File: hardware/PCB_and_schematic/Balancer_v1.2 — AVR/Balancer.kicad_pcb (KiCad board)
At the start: 2 copper layers, 99.5 x 99.5 mm, 198 parts, among them J1 BATT_OUT, J10 RS485, J11 HEATSING_TEMP1, J12 External Current Shunt, J13 BATT_IN, J14 LOAD_RESISTOR, J15 LOAD_RESISTOR, J16 ICP, J3 Conn_01x03, J4 HEATSING_TEMP1, J5 FAN1, J6 FAN2, J7 BATT_12V, J8 Conn_01x06, J9 RS485, Q1 BC817, Q10 BC807, Q11 BC817, Q12 BC817, Q13 BD238, Q14 BC807, Q15 BC817, Q16 BD238, Q18 IRF540N, Q2 BC817, Q23 BC817, Q25 IRF540N, Q3 BC807, Q4 PMOS, Q5 PMOS, Q6 BC817, Q7 BC807, Q8 BC817, Q9 BC817, U1 LM324, U10 PC817, U11 LM7805_TO220, U12 LM317_TO-220, U2 74AHCT125, U4 TL432DBZ, U5 ADUM3211ARZ, U6 ST485, U7 INA226, U8 AVR64DD28, U9 B0505S-1W

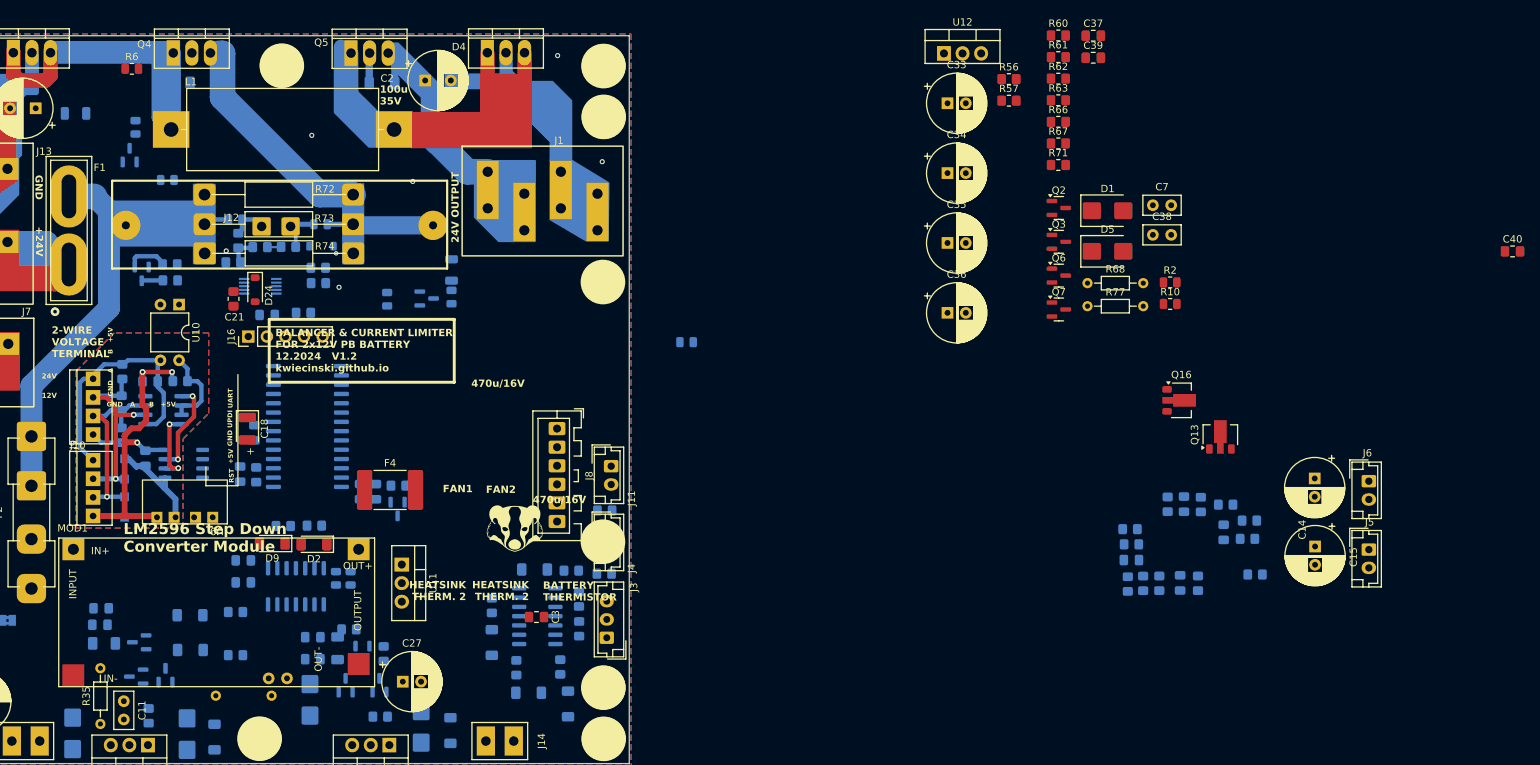
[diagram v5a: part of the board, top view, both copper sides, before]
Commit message: mmc pinout update, change schematic
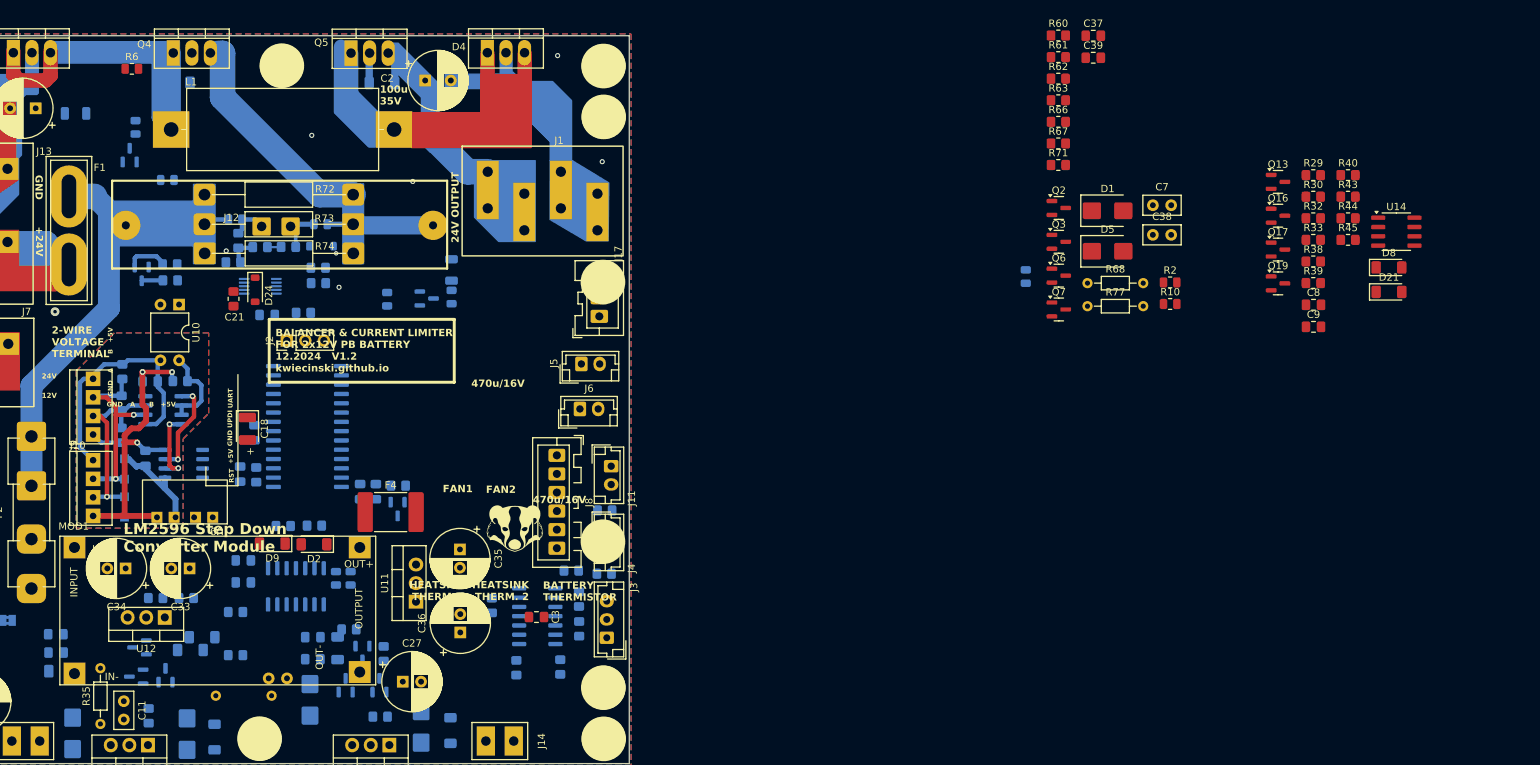
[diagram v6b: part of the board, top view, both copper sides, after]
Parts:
- removed C12, C13, C40: 100n, Capacitor_SMD:C_0805_2012Metric_Pad1.18x1.45mm_HandSolder
- removed C14, C15: 470u/16V, Capacitor_THT:CP_Radial_D8.0mm_P2.50mm
- removed D10, D11, D12, D13: 3V3, Diode_SMD:D_MiniMELF
- removed J16: ICP, Connector_PinHeader_2.54mm:PinHeader_1x05_P2.54mm_Vertical
- removed R46: 6k2, Resistor_SMD:R_0805_2012Metric_Pad1.20x1.40mm_HandSolder
- removed R50: 1k, Resistor_SMD:R_0805_2012Metric_Pad1.20x1.40mm_HandSolder
- added D21: BAT86, Diode_SMD:D_MiniMELF, F.Cu at (360.4, 85.9)
- added D8: BAT86, Diode_SMD:D_MiniMELF, F.Cu at (360.4, 82.6)
- added J17: Conn_01x03, My-Footprints-connectors:JST_XA_1x03_P2.54mm_Vertical, F.Cu at (252.4, 89.2)
- added J2: ICP, Connector_PinHeader_2.54mm:PinHeader_1x03_P2.54mm_Vertical, F.Cu at (209.7, 92.5)
- added Q17: BC817, Package_TO_SOT_SMD:SOT-23, F.Cu at (345.2, 80.1)
- added Q19: AO3400A, Package_TO_SOT_SMD:SOT-23, F.Cu at (345.2, 84.7)
- added U14: LMV358, Package_SO:SOIC-8_3.9x4.9mm_P1.27mm, F.Cu at (361.4, 77.7)
- C8, C9: value 1u -> 47n; moved to F.Cu
- J6: value FAN2 -> FAN1
- Q13: value BD238 -> AO3400A; footprint Package_TO_SOT_SMD:SOT-89-3 -> Package_TO_SOT_SMD:SOT-23
- Q16: value BD238 -> BC817; footprint Package_TO_SOT_SMD:SOT-89-3 -> Package_TO_SOT_SMD:SOT-23
- R29: value 2k2 -> 10k; moved to F.Cu
- R30: value 2k2 -> 210mR; moved to F.Cu
- R32: value 100k -> 100R; moved to F.Cu
- R33: value 100k -> 10k; moved to F.Cu
- R38: value 1k -> 10k; moved to F.Cu
- R39: value 0R -> 10k; moved to F.Cu
- R40: value 0R -> 100R; moved to F.Cu
- R43: value 10K -> 210mR; moved to F.Cu
- R44: value 6k2 -> 1k; moved to F.Cu
- R45: value 10k -> 1k; moved to F.Cu
- R56, R57: moved to B.Cu
- moved R57 135.0 mm to (191.8, 127.8), turned to 180 degrees
- moved R56 133.0 mm to (195.9, 127.8)
- moved U12 131.5 mm to (193.0, 130.4), turned to 180 degrees
- moved C34 124.7 mm to (187.7, 123.7), turned to 180 degrees
- moved C33 121.6 mm to (196.4, 123.7), turned to 180 degrees
- moved J5 110.6 mm to (249.9, 95.8), turned to 0 degrees
- moved J6 108.3 mm to (249.8, 101.9), turned to 0 degrees
- moved C36 79.7 mm to (233.4, 132.4), turned to 90 degrees
- moved C35 78.7 mm to (233.3, 121.1), turned to -90 degrees
- moved R40 61.5 mm to (354.8, 69.9), turned to 0 degrees
- moved R45 54.7 mm to (354.8, 78.8), turned to 0 degrees
- moved R30 51.9 mm to (350.0, 72.9)
- moved R29 49.2 mm to (350.0, 69.9), turned to 0 degrees
- moved R33 48.5 mm to (350.0, 78.8)
- moved R7 47.2 mm to (310.7, 83.8), turned to 90 degrees
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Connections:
- net Net-(J17-Pin_1) renamed /BMS_microcontroller/VOLTAGE_BATT_12V_3W
- C38 pad 2: Net-(D5-A1) -> DC_LINE_24V
- C8 pad 1: Net-(U3B-+) -> GND
- C8 pad 2: GND -> ADC_I_FAN2
- C9 pad 1: Net-(U3A-+) -> GND
- C9 pad 2: GND -> ADC_I_FAN1
- D4 pad 1: Net-(Q5-D) -> Net-(D5-A2)
- D4 pad 3: Net-(Q5-D) -> Net-(D5-A2)
- D5 pad 1: Net-(D5-A1) -> DC_LINE_24V
- J5 pad 1: Net-(J5-Pin_1) -> +12V_LOCAL
- J5 pad 2: GND -> Net-(D8-A2)
- J6 pad 1: Net-(J6-Pin_1) -> +12V_LOCAL
- J6 pad 2: GND -> Net-(D21-A2)
- J8 pad 2: LED3_PA6 -> LED1_PF6_RST
- J8 pad 3: LED4_PA5 -> DBG_UART
- J8 pad 4: DBG_UART -> unconnected-(J8-Pin_4-Pad4)
- J8 pad 5: LED1_PA7 -> unconnected-(J8-Pin_5-Pad5)
- L1 pad 2: Net-(Q5-D) -> Net-(D5-A2)
- Q13 pad 1: Net-(J6-Pin_1) -> Net-(Q13-G)
- Q13 pad 2: +BATT_12V -> Net-(Q13-S)
- Q13 pad 3: Net-(Q13-B) -> Net-(D8-A2)
- Q16 pad 1: Net-(J5-Pin_1) -> Net-(Q16-B)
- Q16 pad 2: +BATT_12V -> GND
- Q16 pad 3: Net-(Q16-B) -> Net-(Q16-C)
- Q5 pad 1: Net-(Q5-D) -> Net-(D5-A2)
- R22 pad 2: TEMP_HEAT_SINK_24V -> TEMP_SMPS
- R23 pad 2: TEMP_HEAT_SINK_12V -> TEMP_BALANCER
- R29 pad 1: PWM_OUT2 -> Net-(Q17-C)
- R29 pad 2: Net-(U3B-+) -> +12V_LOCAL
- R30 pad 1: PWM_OUT1 -> Net-(Q13-S)
- R30 pad 2: Net-(U3A-+) -> GND
- R32 pad 1: GND -> Net-(Q17-C)
- R32 pad 2: Net-(U3B-+) -> Net-(Q13-G)
- R33 pad 1: GND -> PWM_OUT1
- R33 pad 2: Net-(U3A-+) -> Net-(Q17-B)
- R38 pad 1: Net-(Q16-B) -> PWM_OUT2
- R38 pad 2: Net-(C13-Pad1) -> Net-(Q16-B)
- R39 pad 1: Net-(U3B--) -> Net-(Q16-C)
- R39 pad 2: Net-(R39-Pad2) -> +12V_LOCAL
- R40 pad 1: Net-(U3A--) -> Net-(Q16-C)
- R40 pad 2: Net-(R40-Pad2) -> Net-(Q19-G)
- R43 pad 1: Net-(R39-Pad2) -> Net-(Q19-S)
- R43 pad 2: Net-(J6-Pin_1) -> GND
- R44 pad 1: GND -> Net-(Q19-S)
- R44 pad 2: Net-(R39-Pad2) -> ADC_I_FAN2
- R45 pad 1: Net-(R40-Pad2) -> Net-(Q13-S)
- R45 pad 2: Net-(J5-Pin_1) -> ADC_I_FAN1
- U8 pad 1: LED1_PA7 -> ADC_I_FAN1
- U8 pad 10: PWM_OUT2 -> TEMP_SMPS
- U8 pad 11: PWM_OUT1 -> TEMP_BALANCER
- U8 pad 12: DAC -> RS485_OUTPUT_ENABLE
- U8 pad 18: RST -> LED1_PF6_RST
- U8 pad 24: RS485_OUTPUT_ENABLE -> PWM_FAN_BALANCER
- U8 pad 25: LED4_PA5 -> PWM_FAN_SMPS
- U8 pad 3: TEMP_AKU_12V -> ADC_I_FAN2
- U8 pad 8: TEMP_AKU_24V -> TEMP_AKU_12V
- U8 pad 9: TEMP_HEAT_SINK_24V -> TEMP_AKU_24V
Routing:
- net Net-(Q5-D): track 58.2 -> 0.00 mm
- net Net-(D5-A2): track 0.00 -> 58.2 mm

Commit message: balacer routing update
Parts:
- removed D15: 3V3, Diode_SMD:D_MiniMELF
- removed D6: 18V, Diode_SMD:D_MiniMELF
- added D10: 1N4148, Diode_THT:D_DO-35_SOD27_P7.62mm_Horizontal, F.Cu at (222.5, 129.7)
- added D11: SM6T15A, Diode_SMD:D_SMB, B.Cu at (200.3, 57.4)
- D1, D5, R6: moved to B.Cu
- D3: value 18V -> SM6T15A; footprint Diode_SMD:D_MiniMELF -> Diode_SMD:D_SMB
- L1: footprint Inductor_THT:L_Axial_L26.0mm_D11.0mm_P30.48mm_Horizontal_Fastron_77A -> My-Footprints:Inductor_Toroidal
- Q4, Q5: value PMOS -> IRF4905; footprint My-Footprints:TO-220-3_V_Thick_Pads -> Package_TO_SOT_THT:TO-220-3_Vertical
- moved R2 179.7 mm to (165.7, 13.0)
- moved Q2 179.7 mm to (150.4, 2.83)
- moved Q3 179.7 mm to (150.4, 7.45)
- moved C7 139.8 mm to (189.4, 56.4), turned to 90 degrees
- moved D1 138.1 mm to (185.1, 55.6), turned to 90 degrees
- moved R68 130.8 mm to (189.4, 67.9), turned to 90 degrees
- moved R27 120.7 mm to (253.5, 92.1), turned to 180 degrees
- moved R49 112.5 mm to (248.9, 93.3), turned to 0 degrees
- moved R48 112.4 mm to (248.9, 88.7), turned to 180 degrees
- moved C17 109.6 mm to (248.9, 91.0), turned to 0 degrees
- moved D5 102.3 mm to (221.2, 62.2), turned to 180 degrees
- moved R7 98.2 mm to (215.8, 58.5)
- moved R3 75.3 mm to (132.3, 3.86)
- moved Q1 75.3 mm to (139.8, 9.56)
- moved R1 75.3 mm to (144.9, 13.0)
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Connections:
- D3 pad 1: Net-(D1-A1) -> DC_LINE_24V
- D3 pad 2: Net-(D3-A) -> Net-(D3-A2)
- Q4 pad 1: Net-(D1-A2) -> Net-(D11-A2)
- Q4 pad 2: Net-(D3-A) -> Net-(D1-A2)
- Q5 pad 1: Net-(D5-A2) -> Net-(D3-A2)
- Q5 pad 2: Net-(D6-A) -> Net-(D5-A2)
- R6 pad 2: Net-(D3-A) -> Net-(D11-A2)
- R7 pad 2: Net-(D6-A) -> Net-(D3-A2)
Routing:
- net Net-(D5-A2): track 58.2 -> 21.9 mm
- net Net-(D1-A2): track 43.5 -> 12.2 mm
- net Net-(D1-A1): track 49.8 -> 71.5 mm
- net Net-(D6-A): track 4.12 -> 0.00 mm
- net Net-(C7-Pad1): track 0.00 -> 3.94 mm
- net GND: vias 9 -> 7

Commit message: balancer pcb update
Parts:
- removed C22: 100n, Capacitor_SMD:C_0805_2012Metric_Pad1.18x1.45mm_HandSolder
- removed R47: 10k, Resistor_SMD:R_0805_2012Metric_Pad1.20x1.40mm_HandSolder
- added C12: 100n, Capacitor_SMD:C_0805_2012Metric_Pad1.18x1.45mm_HandSolder, B.Cu at (221.9, 103.3)
- added C13: 100n, Capacitor_SMD:C_0805_2012Metric_Pad1.18x1.45mm_HandSolder, B.Cu at (198.4, 119.0)
- added C14: 10u, Capacitor_SMD:C_1206_3216Metric, B.Cu at (198.8, 114.5)
- C18, C21, C37, C39, C8, C9, D21, D24, D8, F4, Q13, Q16, Q17, Q19, Q2, Q3, Q6, Q7, R10, R2, R29, R30, R32, R33, R38, R39, R40, R43, R44, R45, R60, R61, R62, R63, R66, R67, R71, U14: moved to B.Cu
- C4: value 100n -> 10u
- D10: footprint Diode_THT:D_DO-35_SOD27_P7.62mm_Horizontal -> Diode_SMD:D_MiniMELF; moved to B.Cu
- Q18, Q25, U11, U12: footprint Package_TO_SOT_THT:TO-220-3_Vertical -> My-Footprints:TO-220-3_Vertical-little-bigger pads
- Q4, Q5: footprint Package_TO_SOT_THT:TO-220-3_Vertical -> My-Footprints:TO-220-3_V_Thick_Pads
- moved U14 124.3 mm to (237.6, 88.5)
- moved R40 124.2 mm to (236.0, 106.4), turned to -90 degrees
- moved R10 122.8 mm to (208.8, 71.0), turned to 180 degrees
- moved R33 122.7 mm to (229.1, 99.5), turned to -90 degrees
- moved R38 120.7 mm to (232.6, 109.7)
- moved R43 118.7 mm to (240.0, 103.3), turned to 180 degrees
- moved R29 118.1 mm to (234.9, 96.5), turned to 180 degrees
- moved R44 117.8 mm to (241.0, 106.6), turned to -90 degrees
- moved R32 116.7 mm to (235.8, 99.7), turned to -90 degrees
- moved Q16 116.7 mm to (232.7, 106.5), turned to 90 degrees
- moved R39 116.4 mm to (235.1, 103.0), turned to 180 degrees
- moved R45 116.2 mm to (240.5, 99.8), turned to -90 degrees
- moved Q17 114.6 mm to (232.3, 99.7)
- moved C8 112.9 mm to (238.7, 106.6), turned to -90 degrees
- moved C9 112.5 mm to (237.9, 99.8), turned to -90 degrees
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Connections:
- C4 pad 2: UPDI -> GND
- R33 pad 1: PWM_OUT1 -> PWM_FAN_SMPS
- R38 pad 1: PWM_OUT2 -> PWM_FAN_BALANCER
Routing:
- net GND: track 0.00 -> 111.8 mm, vias 7 -> 2
- net +5V: track 0.00 -> 97.3 mm, vias 0 -> 7
- net GNDA: track 18.4 -> 75.6 mm, vias 1 -> 3
- net RS485_OUTPUT_ENABLE: track 0.00 -> 54.3 mm, vias 0 -> 2
- net DC_LINE_24V: track 12.5 -> 62.9 mm
- net Net-(D5-A2): track 21.9 -> 62.0 mm
- net Net-(D1-A2): track 12.2 -> 48.4 mm
- net UPDI: track 0.00 -> 29.9 mm, vias 0 -> 2
- net SDA: track 0.00 -> 28.6 mm, vias 0 -> 2
- net Net-(D1-A1): track 71.5 -> 98.1 mm
- net CLOCK: track 0.00 -> 25.0 mm
- net Net-(D26-A1): track 0.00 -> 24.6 mm
- net +BATT_12V: track 6.76 -> 31.1 mm
- net VREF: track 0.00 -> 20.0 mm
- net RS232_TX: track 0.00 -> 16.9 mm
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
